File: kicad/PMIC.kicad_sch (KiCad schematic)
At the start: 19 parts, among them U3 nPM1300-CAXX

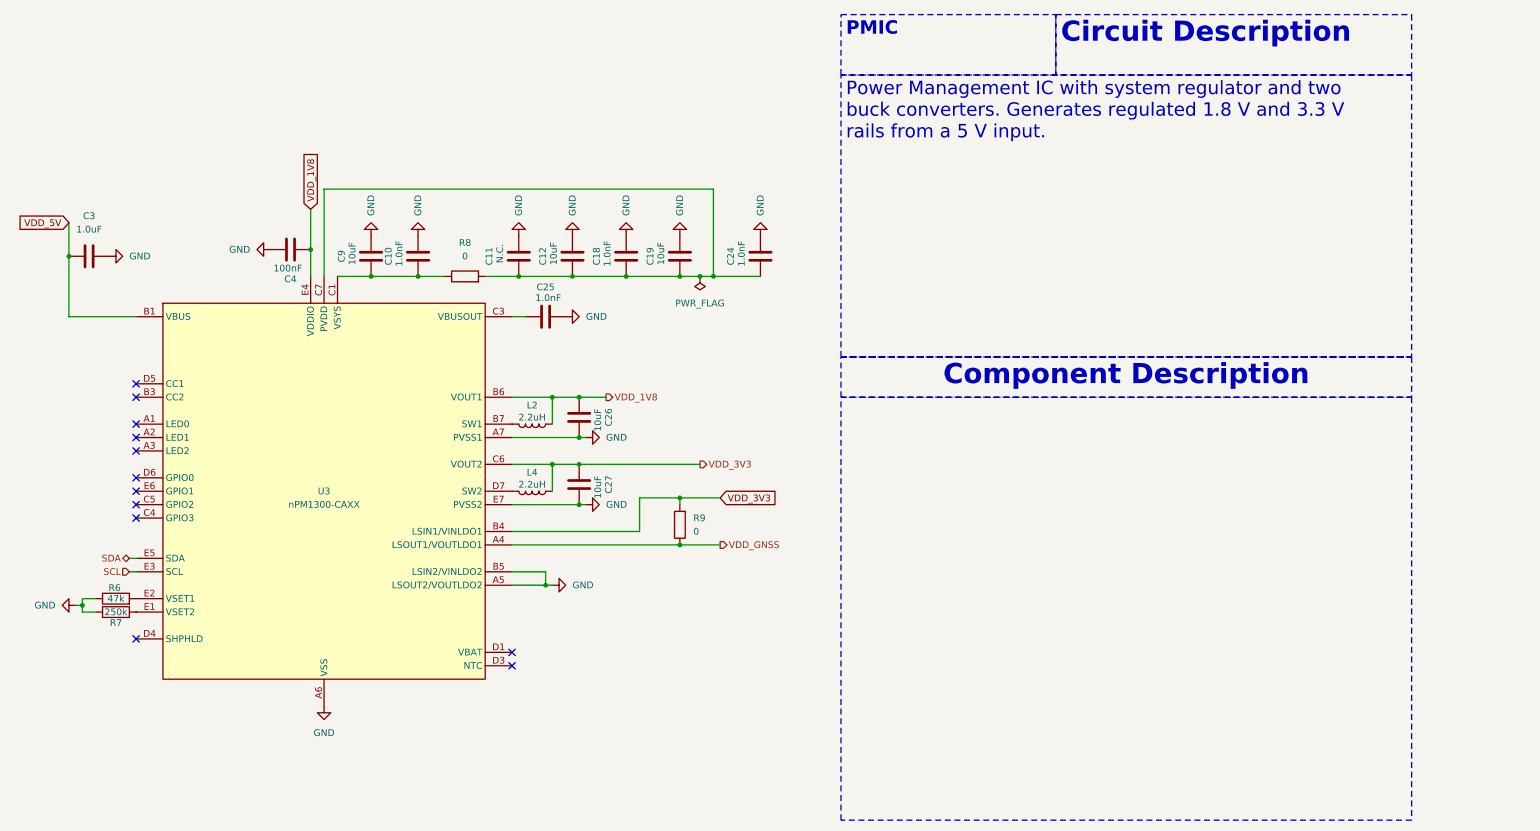
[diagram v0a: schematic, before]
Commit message: docs: update documentation to be more accurate
Signed-off-by: Bobo Bäck Engström <bobo@id8-engineering.io>
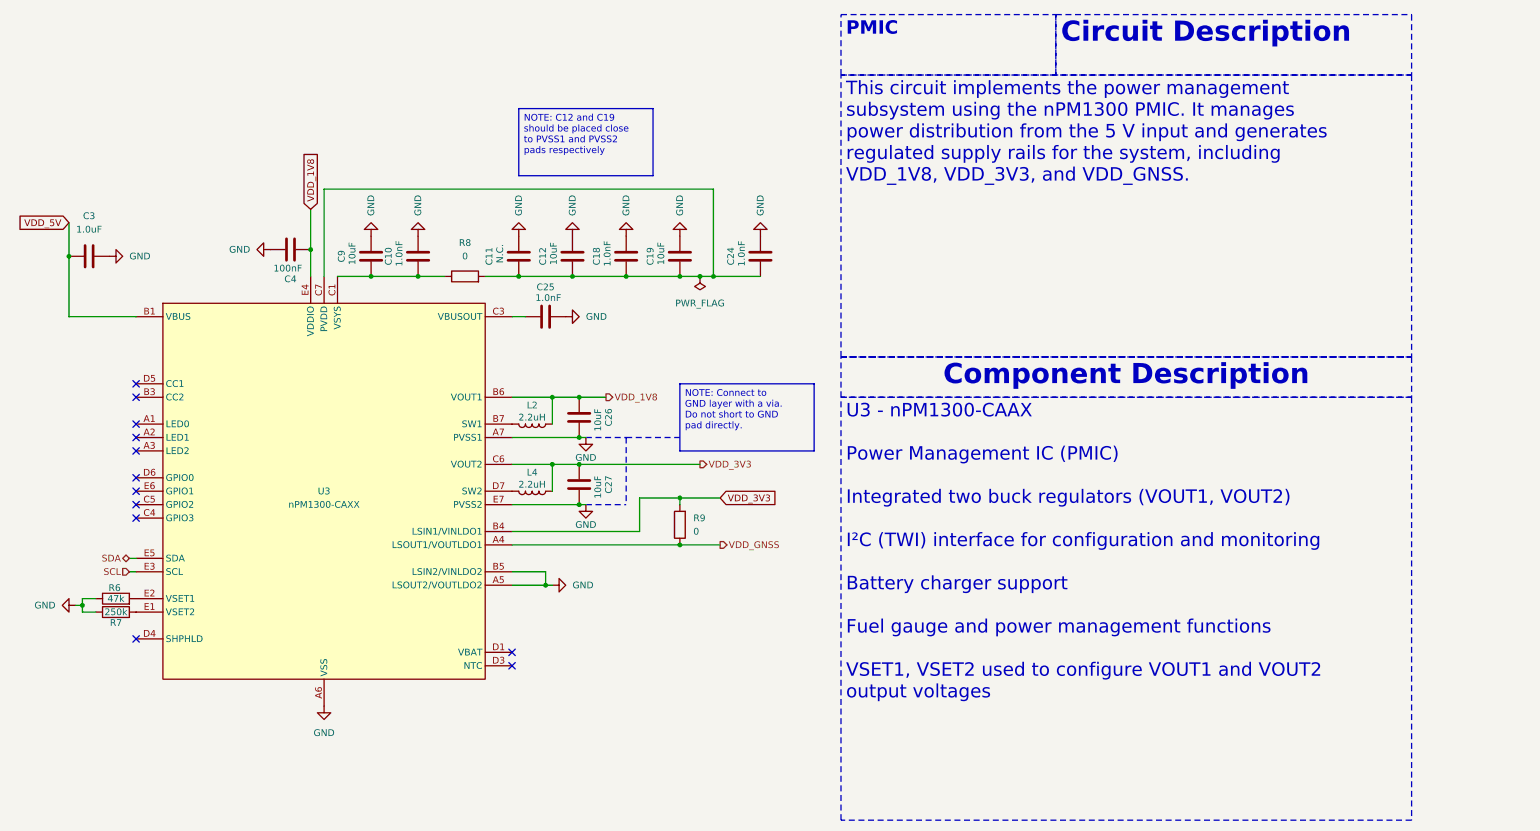
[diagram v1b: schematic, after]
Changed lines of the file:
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@@
 		)
 	)
-	(text_box "Power Management IC with system regulator and two buck converters. Generates regulated 1.8 V and 3.3 V rails from a 5 V input."
+	(text_box "This circuit implements the power management subsystem using the nPM1300 PMIC. It manages power distribution from the 5 V input and generates regulated supply rails for the system, including VDD_1V8, VDD_3V3, and VDD_GNSS."
 		(exclude_from_sim no)
 		(at 176.53 24.13 0)
@@
 		)
 	)
-	(text_box "\n"
+	(text_box "U3 - nPM1300-CAAX\n\nPower Management IC (PMIC)\n\nIntegrated two buck regulators (VOUT1, VOUT2)\n\nI²C (TWI) interface for configuration and monitoring\n\nBattery charger support\n\nFuel gauge and power management functions\n\nVSET1, VSET2 used to configure VOUT1 and VOUT2 output voltages"
 		(exclude_from_sim no)
 		(at 176.53 85.09 0)
@@
 		)
 	)
+	(text_box "NOTE: Connect to\nGND layer with a via.\nDo not short to GND\npad directly."
+		(exclude_from_sim no)
+		(at 146.05 82.55 0)
+		(size 25.4 12.7)
+		(margins 0.9525 0.9525 0.9525 0.9525)
+		(stroke
+			(width 0)
+			(type solid)
+			(color 255 0 0 1)
+		)
+		(fill
+			(type color)
+			(color 255 67 78 1)
+		)
+		(effects
+			(font
+				(size 1.27 1.27)
+				(color 0 0 0 1)
+			)
+			(justify left top)
+		)
+	)
 	(text_box "Circuit Description\n"
 		(exclude_from_sim no)
@@
 		)
 	)
+	(text_box "NOTE: C12 and C19 should be placed close to PVSS1 and PVSS2 pads respectively\n"
+		(exclude_from_sim no)
+		(at 115.57 30.48 0)
+		(size 25.4 12.7)
+		(margins 0.9525 0.9525 0.9525 0.9525)
+		(stroke
+			(width 0)
+			(type solid)
+			(color 255 0 0 1)
+		)
+		(fill
+			(type color)
+			(color 255 67 78 1)
+		)
+		(effects
+			(font
+				(size 1.27 1.27)
+				(color 0 0 0 1)
+			)
+			(justify left top)
+		)
+	)
 	(junction
 		(at 30.48 58.42)
@@
 		)
 	)
+	(polyline
+		(pts
+			(xy 128.27 105.41) (xy 135.89 105.41)
+		)
+		(stroke
+			(width 0)
+			(type dash)
+			(color 255 74 77 1)
+		)
+	)
 	(wire
 		(pts
@@
 		)
 	)
+	(polyline
+		(pts
+			(xy 128.27 92.71) (xy 135.89 92.71)
+		)
+		(stroke
+			(width 0)
+			(type dash)
+			(color 255 74 77 1)
+		)
+	)
 	(wire
 		(pts
@@
 		)
 	)
+	(polyline
+		(pts
+			(xy 135.89 92.71) (xy 146.05 92.71)
+		)
+		(stroke
+			(width 0)
+			(type dash)
+			(color 255 74 77 1)
+		)
+	)
 	(wire
 		(pts
@@
 			(width 0)
 			(type default)
+		)
+	)
+	(polyline
+		(pts
+			(xy 135.89 92.71) (xy 135.89 105.41)
+		)
+		(stroke
+			(width 0)
+			(type dash)
+			(color 255 74 77 1)
 		)
 	)
@@
 	(symbol
 		(lib_id "seven_lib:GND")
-		(at 128.27 92.71 90)
+		(at 128.27 92.71 0)
 		(unit 1)
 		(exclude_from_sim no)
@@
 		(on_board yes)
 		(dnp no)
-		(fields_autoplaced yes)
 		(property "Reference" "#PWR042"
-			(at 134.62 92.71 0)
+			(at 128.27 99.06 0)
 			(effects
 				(font
@@
 		)
 		(property "Value" "GND"
-			(at 132.08 92.7099 90)
-			(effects
-				(font
-					(size 1.27 1.27)
-				)
-				(justify right)
+			(at 128.27 96.52 0)
+			(effects
+				(font
+					(size 1.27 1.27)
+				)
 			)
 		)
@@
 	(symbol
 		(lib_id "seven_lib:GND")
-		(at 128.27 105.41 90)
+		(at 128.27 105.41 0)
 		(unit 1)
 		(exclude_from_sim no)
@@
 		(on_board yes)
 		(dnp no)
-		(fields_autoplaced yes)
 		(property "Reference" "#PWR050"
-			(at 134.62 105.41 0)
+			(at 128.27 111.76 0)
 			(effects
 				(font
@@
 		)
 		(property "Value" "GND"
-			(at 132.08 105.4099 90)
-			(effects
-				(font
-					(size 1.27 1.27)
-				)
-				(justify right)
-			)
-		)
+			(at 128.27 109.22 0)
+			(effects
+				(font
+					(size 1.27 1.27)
+				)
+			)
+		)

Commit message: fix: change C fp to smaller one.
Signed-off-by: Bobo Bäck Engström <bobo@id8-engineering.io>
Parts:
- C10, C11, C12, C18, C19, C24, C25, C26, C27, C3, C4, C9: footprint seven-lib:C_1812_4532Metric -> seven-lib:C_0402_1005Metric
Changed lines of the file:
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@@
 			)
 		)
-		(property "Footprint" "seven-lib:C_1812_4532Metric"
+		(property "Footprint" "seven-lib:C_0402_1005Metric"
 			(at 127.9652 92.71 0)
 			(effects
@@
 			)
 		)
-		(property "Footprint" "seven-lib:C_1812_4532Metric"
+		(property "Footprint" "seven-lib:C_0402_1005Metric"
 			(at 160.3248 54.61 0)
 			(effects
@@
 			)
 		)
-		(property "Footprint" "seven-lib:C_1812_4532Metric"
+		(property "Footprint" "seven-lib:C_0402_1005Metric"
 			(at 127.9652 105.41 0)
 			(effects
@@
 			)
 		)
-		(property "Footprint" "seven-lib:C_1812_4532Metric"
+		(property "Footprint" "seven-lib:C_0402_1005Metric"
 			(at 145.0848 54.61 0)
 			(effects
@@
 			)
 		)
-		(property "Footprint" "seven-lib:C_1812_4532Metric"
+		(property "Footprint" "seven-lib:C_0402_1005Metric"
 			(at 86.6648 54.61 0)
 			(effects
@@
 			)
 		)
-		(property "Footprint" "seven-lib:C_1812_4532Metric"
+		(property "Footprint" "seven-lib:C_0402_1005Metric"
 			(at 68.58 58.1152 0)
 			(effects
@@
 			)
 		)
-		(property "Footprint" "seven-lib:C_1812_4532Metric"
+		(property "Footprint" "seven-lib:C_0402_1005Metric"
 			(at 124.46 68.8848 0)
 			(effects
@@
 			)
 		)
-		(property "Footprint" "seven-lib:C_1812_4532Metric"
+		(property "Footprint" "seven-lib:C_0402_1005Metric"
 			(at 124.7648 54.61 0)
 			(effects
@@
 			)
 		)
-		(property "Footprint" "seven-lib:C_1812_4532Metric"
+		(property "Footprint" "seven-lib:C_0402_1005Metric"
 			(at 95.5548 54.61 0)
 			(effects
@@
 			)
 		)
-		(property "Footprint" "seven-lib:C_1812_4532Metric"
+		(property "Footprint" "seven-lib:C_0402_1005Metric"
 			(at 114.6048 54.61 0)
 			(effects
@@
 			)
 		)
-		(property "Footprint" "seven-lib:C_1812_4532Metric"
+		(property "Footprint" "seven-lib:C_0402_1005Metric"
 			(at 134.9248 54.61 0)
 			(effects
@@
 			)
 		)
-		(property "Footprint" "seven-lib:C_1812_4532Metric"
+		(property "Footprint" "seven-lib:C_0402_1005Metric"
 			(at 38.1 57.4548 0)
 			(effects

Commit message: fix: change R fp to a smaller one
Signed-off-by: Bobo Bäck Engström <bobo@id8-engineering.io>
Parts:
- L2, L4: footprint seven-lib:L_1008_2520Metric -> seven-lib:L_0603_1608Metric
- R6, R7, R8, R9: footprint seven-lib:R_0603_1608Metric -> seven-lib:R_0402_1005Metric
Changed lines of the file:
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@@
 			)
 		)
-		(property "Footprint" "seven-lib:L_1008_2520Metric"
+		(property "Footprint" "seven-lib:L_0603_1608Metric"
 			(at 118.11 90.17 0)
 			(effects
@@
 			)
 		)
-		(property "Footprint" "seven-lib:L_1008_2520Metric"
+		(property "Footprint" "seven-lib:L_0603_1608Metric"
 			(at 118.11 102.87 0)
 			(effects
@@
 			)
 		)
-		(property "Footprint" "seven-lib:R_0603_1608Metric"
+		(property "Footprint" "seven-lib:R_0402_1005Metric"
 			(at 147.828 109.22 90)
 			(effects
@@
 			)
 		)
-		(property "Footprint" "seven-lib:R_0603_1608Metric"
+		(property "Footprint" "seven-lib:R_0402_1005Metric"
 			(at 39.37 124.968 90)
 			(effects
@@
 			)
 		)
-		(property "Footprint" "seven-lib:R_0603_1608Metric"
+		(property "Footprint" "seven-lib:R_0402_1005Metric"
 			(at 105.41 64.008 90)
 			(effects
@@
 			)
 		)
-		(property "Footprint" "seven-lib:R_0603_1608Metric"
+		(property "Footprint" "seven-lib:R_0402_1005Metric"
 			(at 39.37 127.508 90)
 			(effects

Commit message: fix: changes made according to review meeting
Signed-off-by: Bobo Bäck Engström <bobo@id8-engineering.io>
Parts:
- added D2: BAT54KFILM, seven-lib:D_SOD-523, symbol seven_lib:BAT54W
- added R17, R18: 4k7, seven-lib:R_0402_1005Metric, symbol seven_lib:R
- added TP13: VDD_5V, seven-lib:TestPoint_Pad_2.0x2.0mm, symbol seven_lib:TestPoint
- added TP18: VDD_1V8, seven-lib:TestPoint_Pad_2.0x2.0mm, symbol seven_lib:TestPoint
- added TP19: VDD_GNSS, seven-lib:TestPoint_Pad_2.0x2.0mm, symbol seven_lib:TestPoint
- added TP20: VDD_3V3, seven-lib:TestPoint_Pad_2.0x2.0mm, symbol seven_lib:TestPoint
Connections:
- net SCL: now also R18.1
- net SDA: now also R17.1
- net VDD_1V8: now also R17.2, R18.2, TP18.1
- net VDD_3V3: now also D2.1 (A), TP20.1
- net VDD_5V: now also TP13.1
- net VDD_GNSS: now also TP19.1
- new net VDD_JTAG: D2.3 (K)

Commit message: fix: satisfy warnings in pcb
Signed-off-by: Bobo Bäck Engström <bobo@id8-engineering.io>
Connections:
- net VDD_JTAG: now also D2.2 (K); no longer D2.3 (K)
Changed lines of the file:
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@@
 		(pin "2"
-		)
-		(pin "3"
 		)
 		(pin "1"

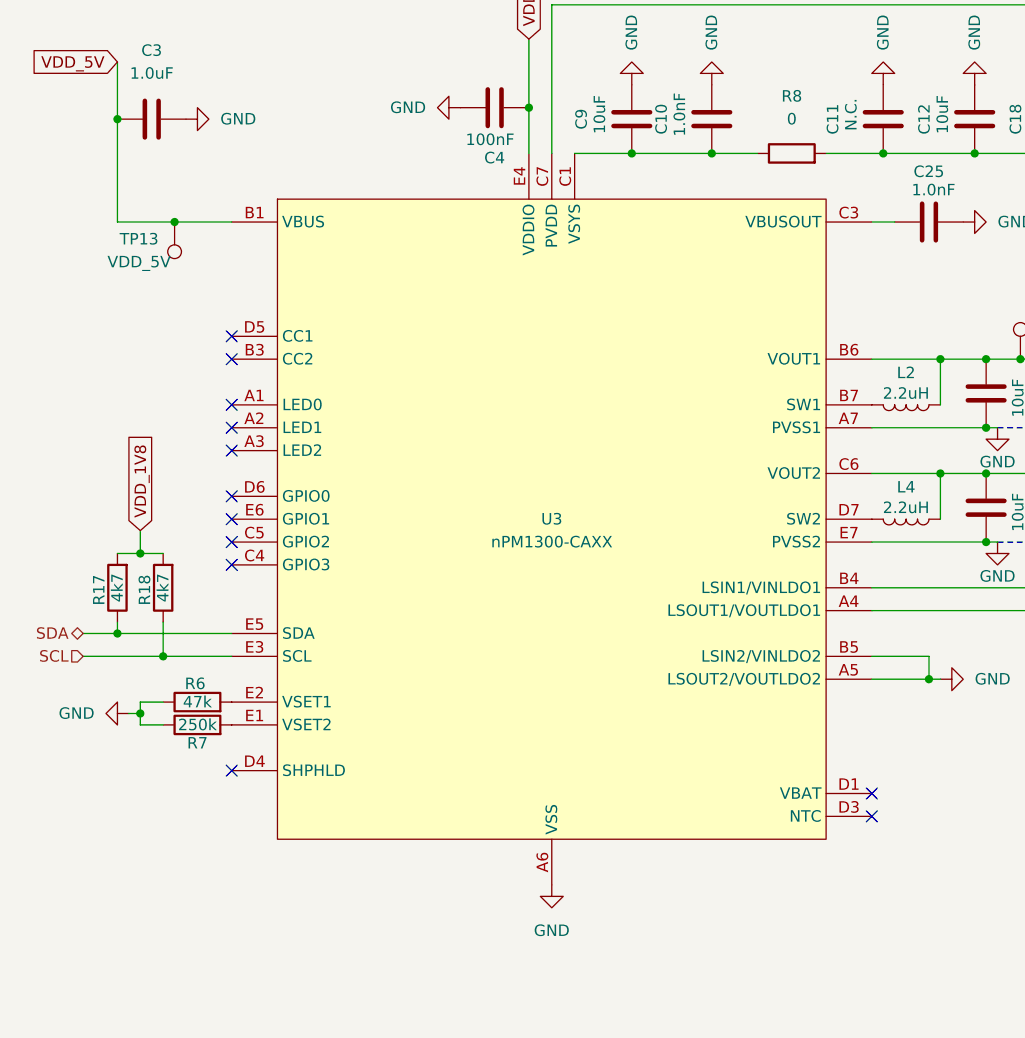
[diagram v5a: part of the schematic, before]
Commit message: feat(PCB): set component-placement example on PCB
This pr will fail due to DRC, skip this and lets have a conversation
about the placement only

Signed-off-by: Bobo Bäck Engström <bobo@id8-engineering.io>
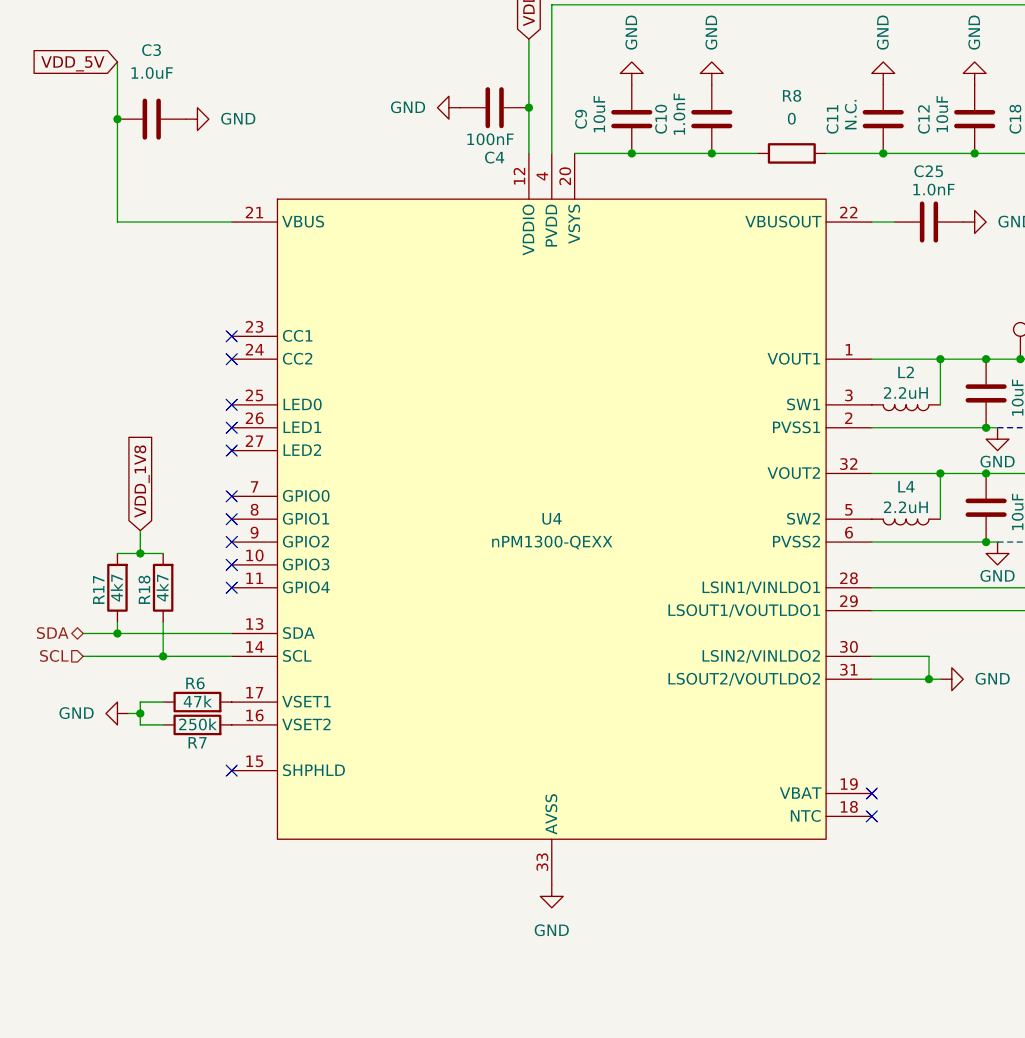
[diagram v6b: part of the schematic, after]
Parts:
- removed TP13: VDD_5V, seven-lib:TestPoint_Pad_2.0x2.0mm, symbol seven_lib:TestPoint
- removed U3: nPM1300-CAXX, seven-lib:BGA-35_7x5_3.077x2.3775mm, symbol seven_lib:nPM1300-CAXX
- added U4: nPM1300-QEXX, seven-lib:QFN-32-1EP_5x5mm_P0.5mm_EP3.6x3.6mm_ThermalVias, symbol seven_lib:nPM1300-QEXX
- C10, C18, C24, C25: MPN (none) -> GRM155R71C102KA01D
- C12, C19, C26, C27, C9: footprint seven-lib:C_0402_1005Metric -> seven-lib:C_0805_2012Metric; MPN (none) -> GRM21BR61A106KE51L
- C3: footprint seven-lib:C_0402_1005Metric -> seven-lib:C_0603_1608Metric; MPN (none) -> GRM188R71C105KA12D
- C4: MPN (none) -> GRM155R71C104KA88D
- D2: MPN (none) -> BAT54KFILM
- L2, L4: footprint seven-lib:L_0603_1608Metric -> seven-lib:L_0805_2012Metric; MPN (none) -> MLP2016V2R2MT0S1
- R17, R18: MPN (none) -> RC0402FR-074K7L
- R6: MPN (none) -> RC0402FR-0747KL
- R7: MPN (none) -> RC0402FR-07250K
- R8, R9: MPN (none) -> RC0402FR-070RL
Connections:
- net GND: now also U4.2 (PVSS1), U4.30 (LSIN2/VINLDO2), U4.31 (LSOUT2/VOUTLDO2), U4.33 (AVSS), U4.6 (PVSS2)
- net SCL: now also U4.14 (SCL)
- net SDA: now also U4.13 (SDA)
- net VDD_1V8: now also U4.1 (VOUT1), U4.12 (VDDIO)
- net VDD_3V3: now also U4.28 (LSIN1/VINLDO1), U4.32 (VOUT2)
- net VDD_5V: now also U4.21 (VBUS)
- net VDD_GNSS: now also U4.29 (LSOUT1/VOUTLDO1)
- net at C11.1, C12.1, C18.1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: now also U4.4 (PVDD)
- net at L2.2: now also U4.3 (SW1)
- net at C10.1, C9.1, R8.1: now also U4.20 (VSYS)
- net at C25.1: now also U4.22 (VBUSOUT)
- net at L4.2: now also U4.5 (SW2)
- net at R7.2: now also U4.16 (VSET2)
- net at R6.2: now also U4.17 (VSET1)
- no-connect marks 12 -> 13

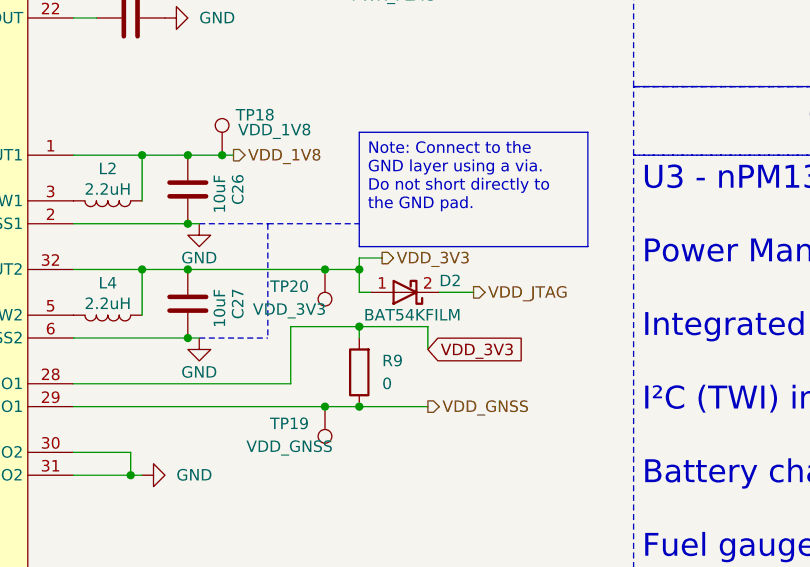
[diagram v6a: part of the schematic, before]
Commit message: fix: fix issues from seven prototype 1
see https://github.com/id8-engineering/seven-bringup/issues/22

Signed-off-by: Bobo Bäck Engström <bobo@id8-engineering.io>
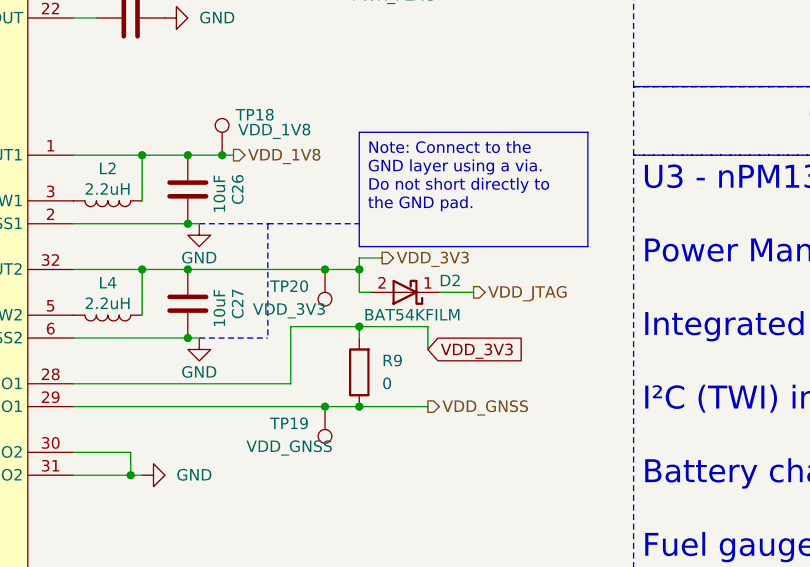
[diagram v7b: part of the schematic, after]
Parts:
- C12, C19, C26, C27, C9: MPN GRM21BR61A106KE51L -> CL21A106KAYNNNE
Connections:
- net VDD_3V3: now also D2.2 (K); no longer D2.1 (A)
- net VDD_JTAG: now also D2.1 (A); no longer D2.2 (K)
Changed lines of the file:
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@@
 			)
 		)
-		(property "MPN" "GRM21BR61A106KE51L"
+		(property "MPN" "CL21A106KAYNNNE"
 			(at 127 88.9 90)
 			(hide yes)
@@
 			)
 		)
-		(property "MPN" "GRM21BR61A106KE51L"
+		(property "MPN" "CL21A106KAYNNNE"
 			(at 127 101.6 90)
 			(hide yes)
@@
 			)
 		)
-		(property "MPN" "GRM21BR61A106KE51L"
+		(property "MPN" "CL21A106KAYNNNE"
 			(at 146.05 58.42 90)
 			(hide yes)
@@
 			)
 		)
-		(property "MPN" "GRM21BR61A106KE51L"
+		(property "MPN" "CL21A106KAYNNNE"
 			(at 87.63 58.42 90)
 			(hide yes)
@@
 			)
 		)
-		(property "MPN" "GRM21BR61A106KE51L"
+		(property "MPN" "CL21A106KAYNNNE"
 			(at 125.73 58.42 90)
 			(hide yes)
